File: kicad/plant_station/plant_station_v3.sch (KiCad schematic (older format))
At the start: 15 parts, among them J10 I2C HOST, J2 MB_I2C, J3 MB_I2C, J4 ZF5S-20-01-T-WT-TR, J5 MB_I2C, J6 MB_I2C, J9 I2C SCREEN

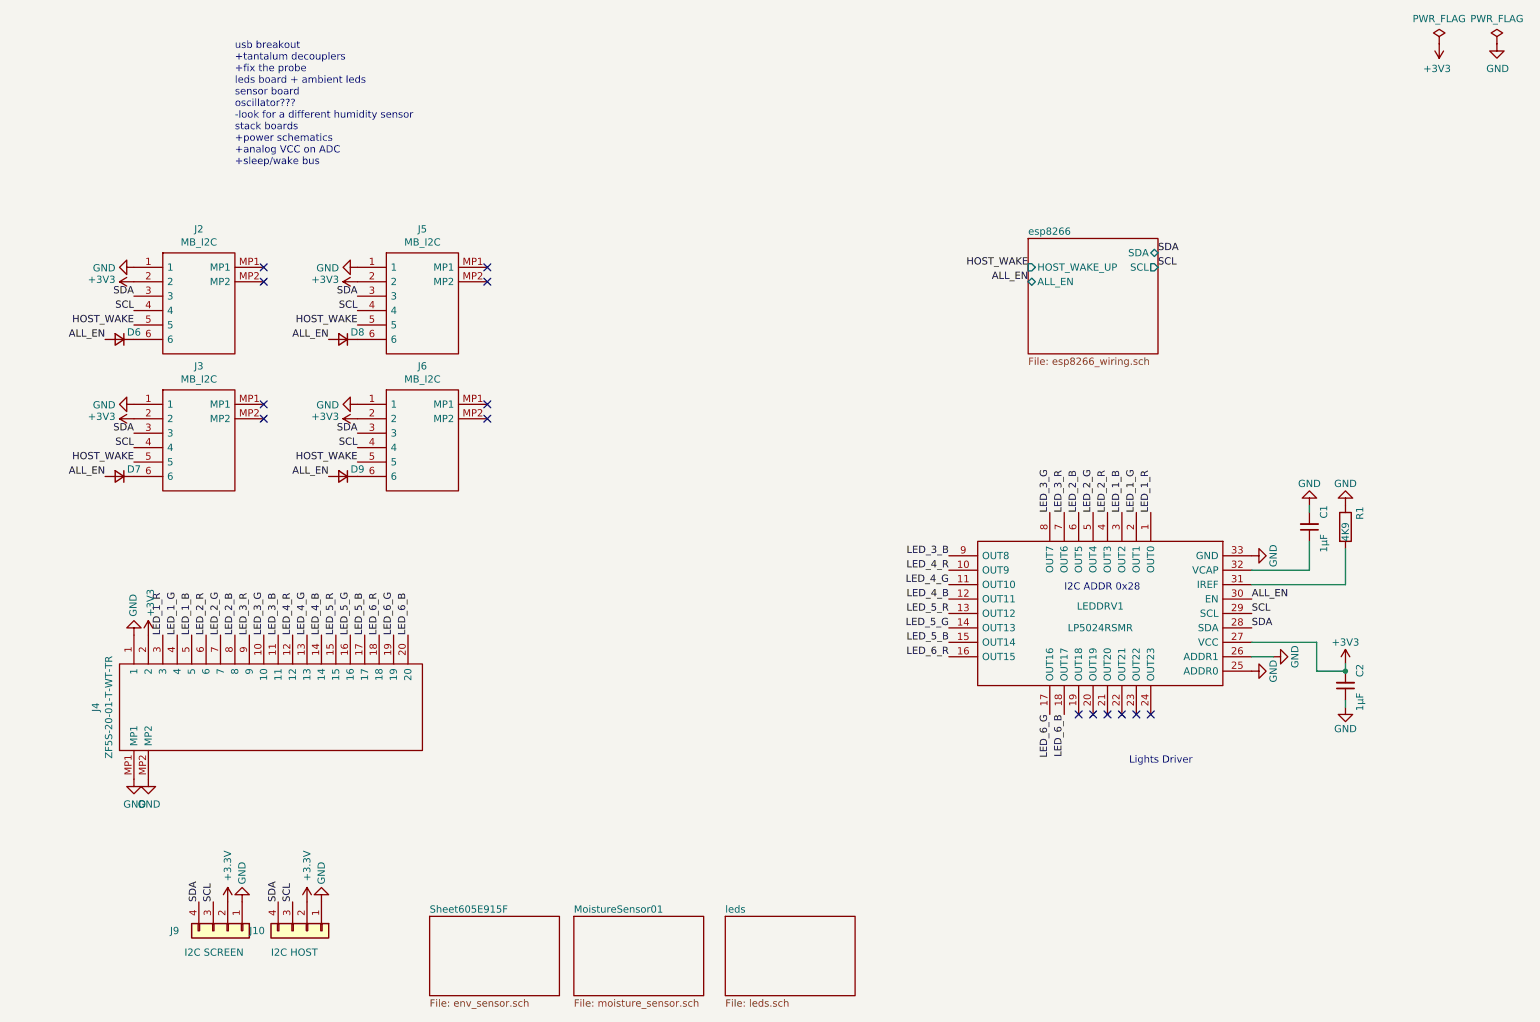
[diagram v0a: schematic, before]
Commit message: v3 schematics complete, USB breakout PCB designed
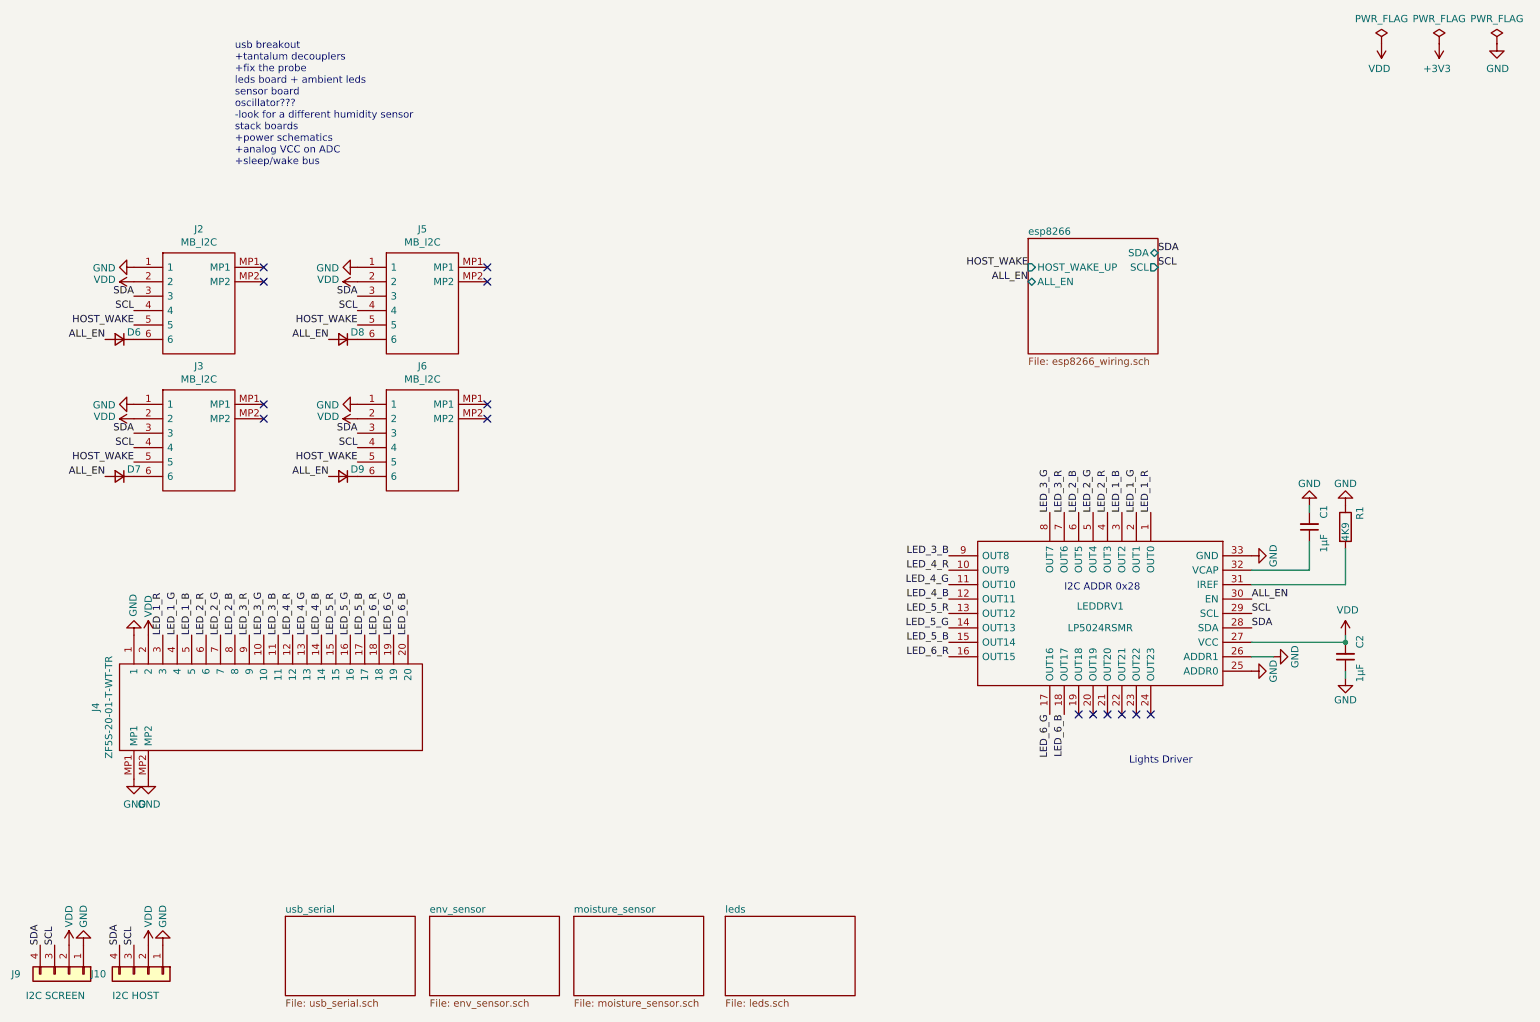
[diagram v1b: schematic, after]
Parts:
- D6, D7, D8, D9: value D_Small -> LS4148
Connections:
- net +3V3: no longer C2.2, J10.2 (Pin_2), J2.2, J3.2, J4.2, J5.2, J6.2, J9.2 (Pin_2), LEDDRV1.27 (VCC)
- new net VDD: C2.2, J10.2 (Pin_2), J2.2, J3.2, J4.2, J5.2, J6.2, J9.2 (Pin_2), LEDDRV1.27 (VCC)
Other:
- moved on the sheet: C2, J10, J9

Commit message: Moved the LED driver to LEDs board, refactored connectors. Hopefuly PCBNEW could update it all in place
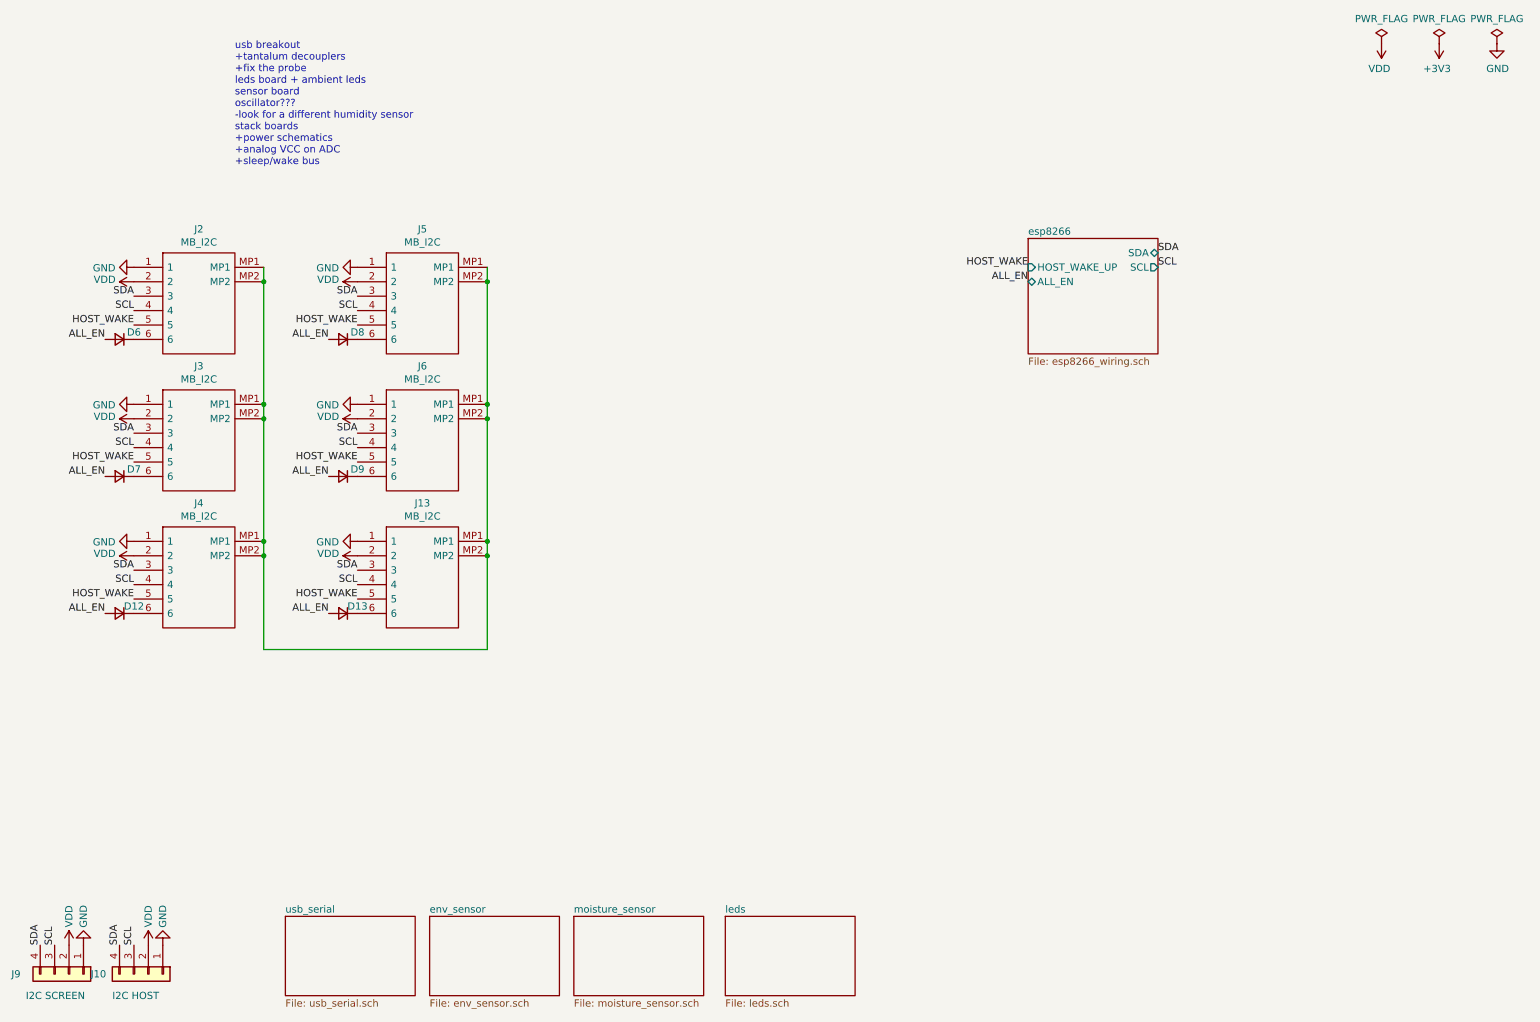
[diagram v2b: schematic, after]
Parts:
- removed C1, C2: 1μF, Capacitor_SMD:C_1206_3216Metric, symbol Device:C_Small
- removed J4: ZF5S-20-01-T-WT-TR, Parts:ZF5S2001TWTTR, symbol Parts:ZF5S-20-01-T-WT-TR
- removed LEDDRV1: LP5024RSMR, SamacSys:QFN40P400X400X100-33N-D, symbol SamaSys:LP5024RSMR
- removed R1: 4K9, Resistor_SMD:R_0805_2012Metric, symbol Device:R
- added D12, D13: LS4148, Parts:MELF_SOD_80_3_BZT55B13GS08, symbol Device:D_Small
- added J13, J4: MB_I2C, Parts:Molex_Conn_SMD_01x06_505567_0671, symbol Parts:505567-0671
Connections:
- net ALL_EN: now also D12.2 (A), D13.2 (A)
- net GND: now also J13.1, J4.1
- net HOST_WAKE: now also J13.5, J4.5
- net SCL: now also J13.4, J4.4
- net SDA: now also J13.3, J4.3
- net VDD: now also J13.2, J4.2
- net at J2.MP1: now also J2.MP2, J3.MP1, J3.MP2, J5.MP1, J5.MP2, J6.MP1, J6.MP2, J13.MP1, J13.MP2, J4.MP1, J4.MP2
- new net: D12.1 (K), J4.6
- new net: D13.1 (K), J13.6
- no-connect marks 14 -> 0
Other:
- note removed: "I2C ADDR 0x28"
- note removed: "Lights Driver"

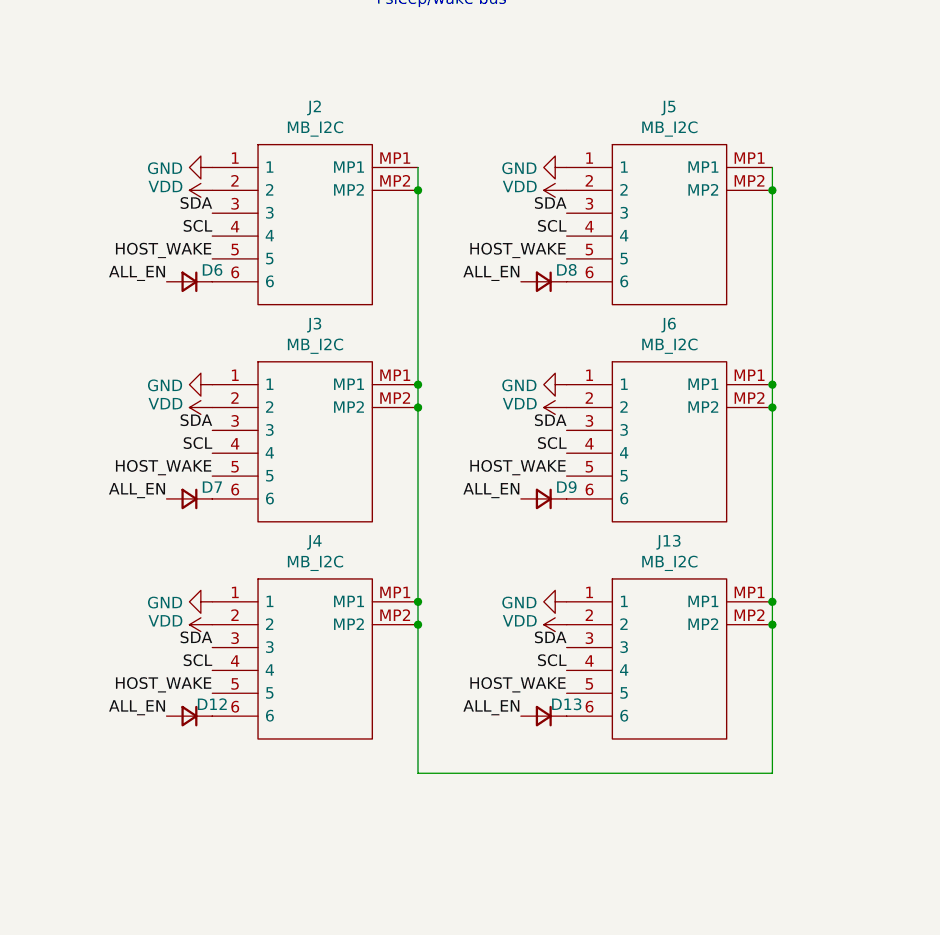
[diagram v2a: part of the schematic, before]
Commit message: Initial board layout complete
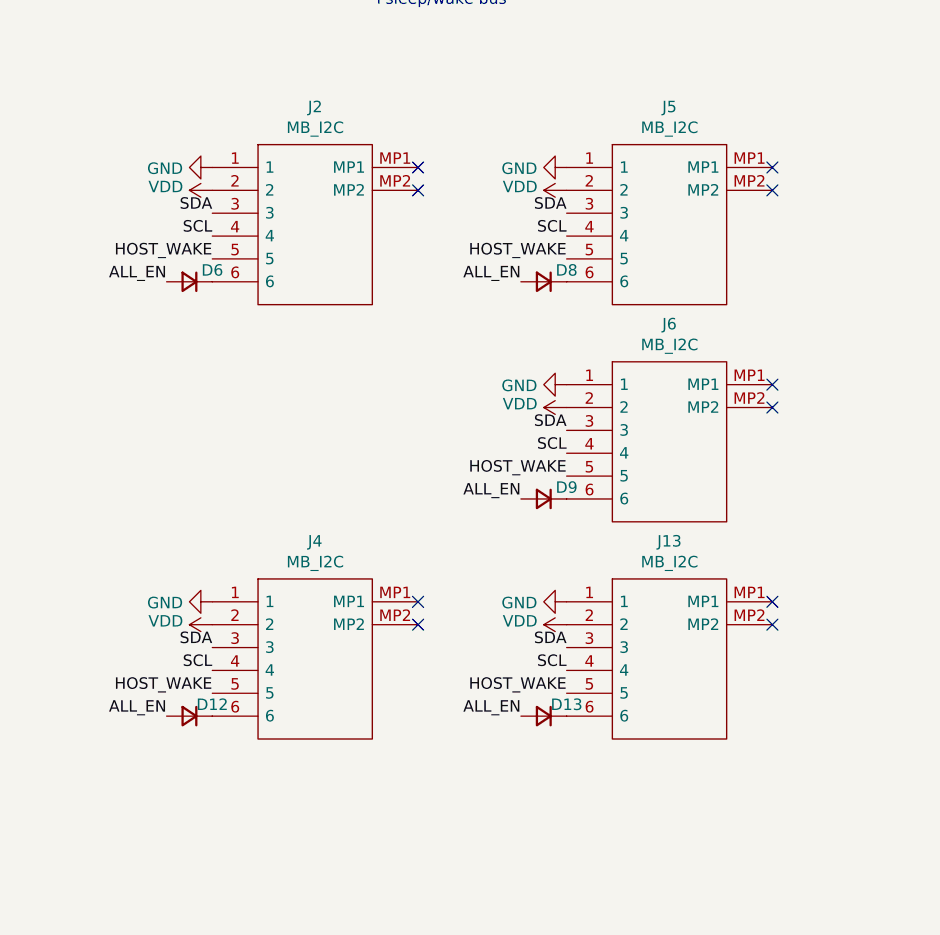
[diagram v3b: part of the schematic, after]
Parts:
- removed D7: LS4148, Parts:MELF_SOD_80_3_BZT55B13GS08, symbol Device:D_Small
- removed J3: MB_I2C, Parts:Molex_Conn_SMD_01x06_505567_0671, symbol Parts:505567-0671
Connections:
- now unconnected: J13.MP1, J13.MP2, J2.MP1, J2.MP2, J4.MP1, J4.MP2, J5.MP1, J5.MP2, J6.MP1, J6.MP2
- no-connect marks 0 -> 10
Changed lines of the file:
@@
-HOST_WAKE
-$Comp
-L Parts:505567-0671 J5
-U 1 1 60493E8D
-P 3050 2350
-F 0 "J5" H 3500 2615 50  0000 C CNN
-F 1 "MB_I2C" H 3500 2524 50  0000 C CNN
-F 2 "Parts:Molex_Conn_SMD_01x06_505567_0671" H 3800 2450 50  0001 L CNN
-F 3 "https://componentsearchengine.com/Datasheets/1/505567-0671.pdf" H 3800 2350 50  0001 L CNN
-F 4 "Molex Micro-Lock PLUS 505567, 1.25mm Pitch, 6 Way, 1 Row, Right Angle PCB Header, Surface Mount" H 3800 2250 50  0001 L CNN "Description"
-F 5 "4.2" H 3800 2150 50  0001 L CNN "Height"
-F 6 "Molex" H 3800 2050 50  0001 L CNN "Manufacturer_Name"
-F 7 "505567-0671" H 3800 1950 50  0001 L CNN "Manufacturer_Part_Number"
-F 8 "505567-0671" H 3800 1850 50  0001 L CNN "Arrow Part Number"
-F 9 "" H 3800 1750 50  0001 L CNN "Arrow Price/Stock"
-F 10 "538-505567-0671" H 3800 1650 50  0001 L CNN "Mouser Part Number"
-F 11 "https://www.mouser.co.uk/ProductDetail/Molex/505567-0671?qs=gt1LBUVyoHmQuimOt9l14w%3D%3D" H 3800 1550 50  0001 L CNN "Mouser Price/Stock"
-	1    3050 2350
-	1    0    0    -1
-$EndComp
-$Comp
-L power:GND #PWR03
-U 1 1 6049521E
-P 1500 3300
-F 0 "#PWR03" H 1500 3050 50  0001 C CNN
-F 1 "GND" V 1505 3172 50  0000 R CNN
-F 2 "" H 1500 3300 50  0001 C CNN
-F 3 "" H 1500 3300 50  0001 C CNN
-	1    1500 3300
-	0    1    1    0
-$EndComp
-Text Label 1500 3500 2    50   ~ 0
-SDA
-Text Label 1500 3600 2    50   ~ 0
-SCL
-Text Label 1300 3800 2    50   ~ 0
-ALL_EN
-$Comp
-L Device:D_Small D7
-U 1 1 6049522D
-P 1400 3800
-F 0 "D7" H 1300 3750 50  0000 C CNN
-F 1 "LS4148" H 1400 3916 50  0001 C CNN
-F 2 "Parts:MELF_SOD_80_3_BZT55B13GS08" V 1400 3800 50  0001 C CNN
-F 3 "~" V 1400 3800 50  0001 C CNN
-	1    1400 3800
-	-1   0    0    1
-$EndComp
-Text Label 1500 3700 2    50   ~ 0
 HOST_WAKE
 $Comp
@@
 Text Label 3050 3700 2    50   ~ 0
 HOST_WAKE
-$Comp
-L Parts:505567-0671 J6
-U 1 1 60496855
-P 3050 3300
-F 0 "J6" H 3500 3565 50  0000 C CNN
-F 1 "MB_I2C" H 3500 3474 50  0000 C CNN
-F 2 "Parts:Molex_Conn_SMD_01x06_505567_0671" H 3800 3400 50  0001 L CNN
-F 3 "https://componentsearchengine.com/Datasheets/1/505567-0671.pdf" H 3800 3300 50  0001 L CNN
-F 4 "Molex Micro-Lock PLUS 505567, 1.25mm Pitch, 6 Way, 1 Row, Right Angle PCB Header, Surface Mount" H 3800 3200 50  0001 L CNN "Description"
-F 5 "4.2" H 3800 3100 50  0001 L CNN "Height"
-F 6 "Molex" H 3800 3000 50  0001 L CNN "Manufacturer_Name"
-F 7 "505567-0671" H 3800 2900 50  0001 L CNN "Manufacturer_Part_Number"
-F 8 "505567-0671" H 3800 2800 50  0001 L CNN "Arrow Part Number"
-F 9 "" H 3800 2700 50  0001 L CNN "Arrow Price/Stock"
-F 10 "538-505567-0671" H 3800 2600 50  0001 L CNN "Mouser Part Number"
-F 11 "https://www.mouser.co.uk/ProductDetail/Molex/505567-0671?qs=gt1LBUVyoHmQuimOt9l14w%3D%3D" H 3800 2500 50  0001 L CNN "Mouser Price/Stock"
-	1    3050 3300
-	1    0    0    -1
-$EndComp
 $Sheet
 S 3550 6850 900  550
@@
 $EndComp
 $Comp
-L power:VDD #PWR07
-U 1 1 5F9FC28C
-P 1500 3400
-F 0 "#PWR07" H 1500 3250 50  0001 C CNN
-F 1 "VDD" V 1515 3527 50  0000 L CNN
-F 2 "" H 1500 3400 50  0001 C CNN
-F 3 "" H 1500 3400 50  0001 C CNN
-	1    1500 3400
-	0    -1   -1   0
-$EndComp
-$Comp
 L power:VDD #PWR021
 U 1 1 5F9FC6B2
@@
 $EndComp
 $Comp
-L Parts:505567-0671 J3
-U 1 1 6049523C
-P 1500 3300
-F 0 "J3" H 1950 3565 50  0000 C CNN
-F 1 "MB_I2C" H 1950 3474 50  0000 C CNN
-F 2 "Parts:Molex_Conn_SMD_01x06_505567_0671" H 2250 3400 50  0001 L CNN
-F 3 "https://componentsearchengine.com/Datasheets/1/505567-0671.pdf" H 2250 3300 50  0001 L CNN
-F 4 "Molex Micro-Lock PLUS 505567, 1.25mm Pitch, 6 Way, 1 Row, Right Angle PCB Header, Surface Mount" H 2250 3200 50  0001 L CNN "Description"
-F 5 "4.2" H 2250 3100 50  0001 L CNN "Height"
-F 6 "Molex" H 2250 3000 50  0001 L CNN "Manufacturer_Name"
-F 7 "505567-0671" H 2250 2900 50  0001 L CNN "Manufacturer_Part_Number"
-F 8 "505567-0671" H 2250 2800 50  0001 L CNN "Arrow Part Number"
-F 9 "" H 2250 2700 50  0001 L CNN "Arrow Price/Stock"
-F 10 "538-505567-0671" H 2250 2600 50  0001 L CNN "Mouser Part Number"
-F 11 "https://www.mouser.co.uk/ProductDetail/Molex/505567-0671?qs=gt1LBUVyoHmQuimOt9l14w%3D%3D" H 2250 2500 50  0001 L CNN "Mouser Price/Stock"
-	1    1500 3300
-	1    0    0    -1
-$EndComp
-Wire Wire Line
-	2400 2350 2400 2450
-Wire Wire Line
-	2400 5000 3950 5000
-Wire Wire Line
-	3950 5000 3950 4350
-Connection ~ 2400 2450
-Wire Wire Line
-	2400 2450 2400 3300
-Connection ~ 2400 3300
-Wire Wire Line
-	2400 3300 2400 3400
-Connection ~ 2400 3400
-Wire Wire Line
-	2400 3400 2400 4250
-Connection ~ 2400 4250
-Wire Wire Line
-	2400 4250 2400 4350
-Connection ~ 2400 4350
-Wire Wire Line
-	2400 4350 2400 5000
-Connection ~ 3950 2450
-Wire Wire Line
-	3950 2450 3950 2350
-Connection ~ 3950 3300
-Wire Wire Line
-	3950 3300 3950 2450
-Connection ~ 3950 3400
-Wire Wire Line
-	3950 3400 3950 3300
-Connection ~ 3950 4250
-Wire Wire Line
-	3950 4250 3950 3400
-Connection ~ 3950 4350
-Wire Wire Line
-	3950 4350 3950 4250
+L Parts:505567-0671 J5
+U 1 1 60493E8D
+P 3050 2350
+F 0 "J5" H 3500 2615 50  0000 C CNN
+F 1 "MB_I2C" H 3500 2524 50  0000 C CNN
+F 2 "Parts:Molex_Conn_SMD_01x06_505567_0671" H 3800 2450 50  0001 L CNN
+F 3 "https://componentsearchengine.com/Datasheets/1/505567-0671.pdf" H 3800 2350 50  0001 L CNN
+F 4 "Molex Micro-Lock PLUS 505567, 1.25mm Pitch, 6 Way, 1 Row, Right Angle PCB Header, Surface Mount" H 3800 2250 50  0001 L CNN "Description"
+F 5 "4.2" H 3800 2150 50  0001 L CNN "Height"
+F 6 "Molex" H 3800 2050 50  0001 L CNN "Manufacturer_Name"
+F 7 "505567-0671" H 3800 1950 50  0001 L CNN "Manufacturer_Part_Number"
+F 8 "505567-0671" H 3800 1850 50  0001 L CNN "Arrow Part Number"
+F 9 "" H 3800 1750 50  0001 L CNN "Arrow Price/Stock"
+F 10 "538-505567-0671" H 3800 1650 50  0001 L CNN "Mouser Part Number"
+F 11 "https://www.mouser.co.uk/ProductDetail/Molex/505567-0671?qs=gt1LBUVyoHmQuimOt9l14w%3D%3D" H 3800 1550 50  0001 L CNN "Mouser Price/Stock"
+	1    3050 2350
+	1    0    0    -1
+$EndComp
+$Comp
+L Parts:505567-0671 J6
+U 1 1 60496855
+P 3050 3300
+F 0 "J6" H 3500 3565 50  0000 C CNN
+F 1 "MB_I2C" H 3500 3474 50  0000 C CNN
+F 2 "Parts:Molex_Conn_SMD_01x06_505567_0671" H 3800 3400 50  0001 L CNN
+F 3 "https://componentsearchengine.com/Datasheets/1/505567-0671.pdf" H 3800 3300 50  0001 L CNN
+F 4 "Molex Micro-Lock PLUS 505567, 1.25mm Pitch, 6 Way, 1 Row, Right Angle PCB Header, Surface Mount" H 3800 3200 50  0001 L CNN "Description"
+F 5 "4.2" H 3800 3100 50  0001 L CNN "Height"
+F 6 "Molex" H 3800 3000 50  0001 L CNN "Manufacturer_Name"
+F 7 "505567-0671" H 3800 2900 50  0001 L CNN "Manufacturer_Part_Number"
+F 8 "505567-0671" H 3800 2800 50  0001 L CNN "Arrow Part Number"
+F 9 "" H 3800 2700 50  0001 L CNN "Arrow Price/Stock"
+F 10 "538-505567-0671" H 3800 2600 50  0001 L CNN "Mouser Part Number"
+F 11 "https://www.mouser.co.uk/ProductDetail/Molex/505567-0671?qs=gt1LBUVyoHmQuimOt9l14w%3D%3D" H 3800 2500 50  0001 L CNN "Mouser Price/Stock"
+	1    3050 3300
+	1    0    0    -1
+$EndComp
+NoConn ~ 3950 2350
+NoConn ~ 3950 2450
+NoConn ~ 3950 3300
+NoConn ~ 3950 3400
+NoConn ~ 3950 4250
+NoConn ~ 3950 4350
+NoConn ~ 2400 4350
+NoConn ~ 2400 4250
+NoConn ~ 2400 2450
+NoConn ~ 2400 2350
 $EndSCHEMATC
